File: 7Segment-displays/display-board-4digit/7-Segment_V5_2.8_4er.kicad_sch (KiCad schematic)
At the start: 3 parts, among them J1 Conn_02x08_Odd_Even, U1 HDSM-443B_CC_2Digit_7Segment_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, U2 HDSM-443B_CC_2Digit_7Segment_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

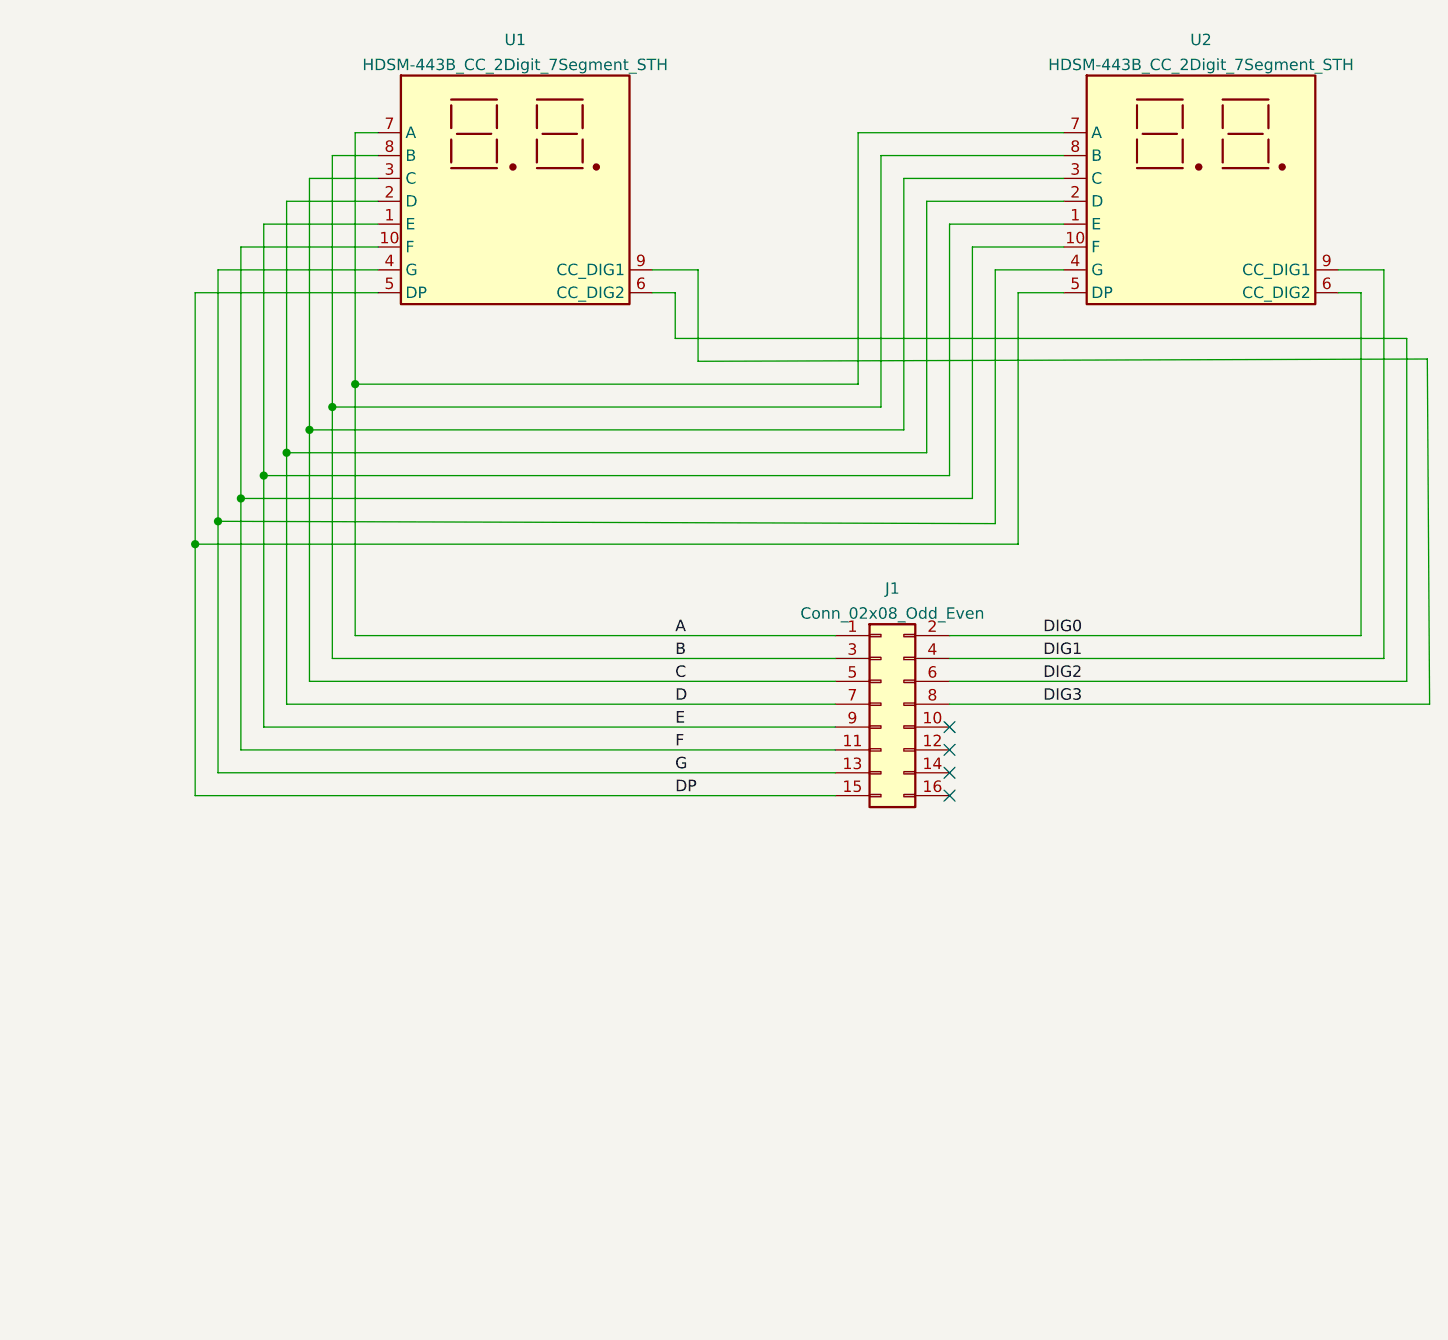
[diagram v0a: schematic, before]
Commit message: new symbol and footprint, connector rotated by 180 degree, new routing
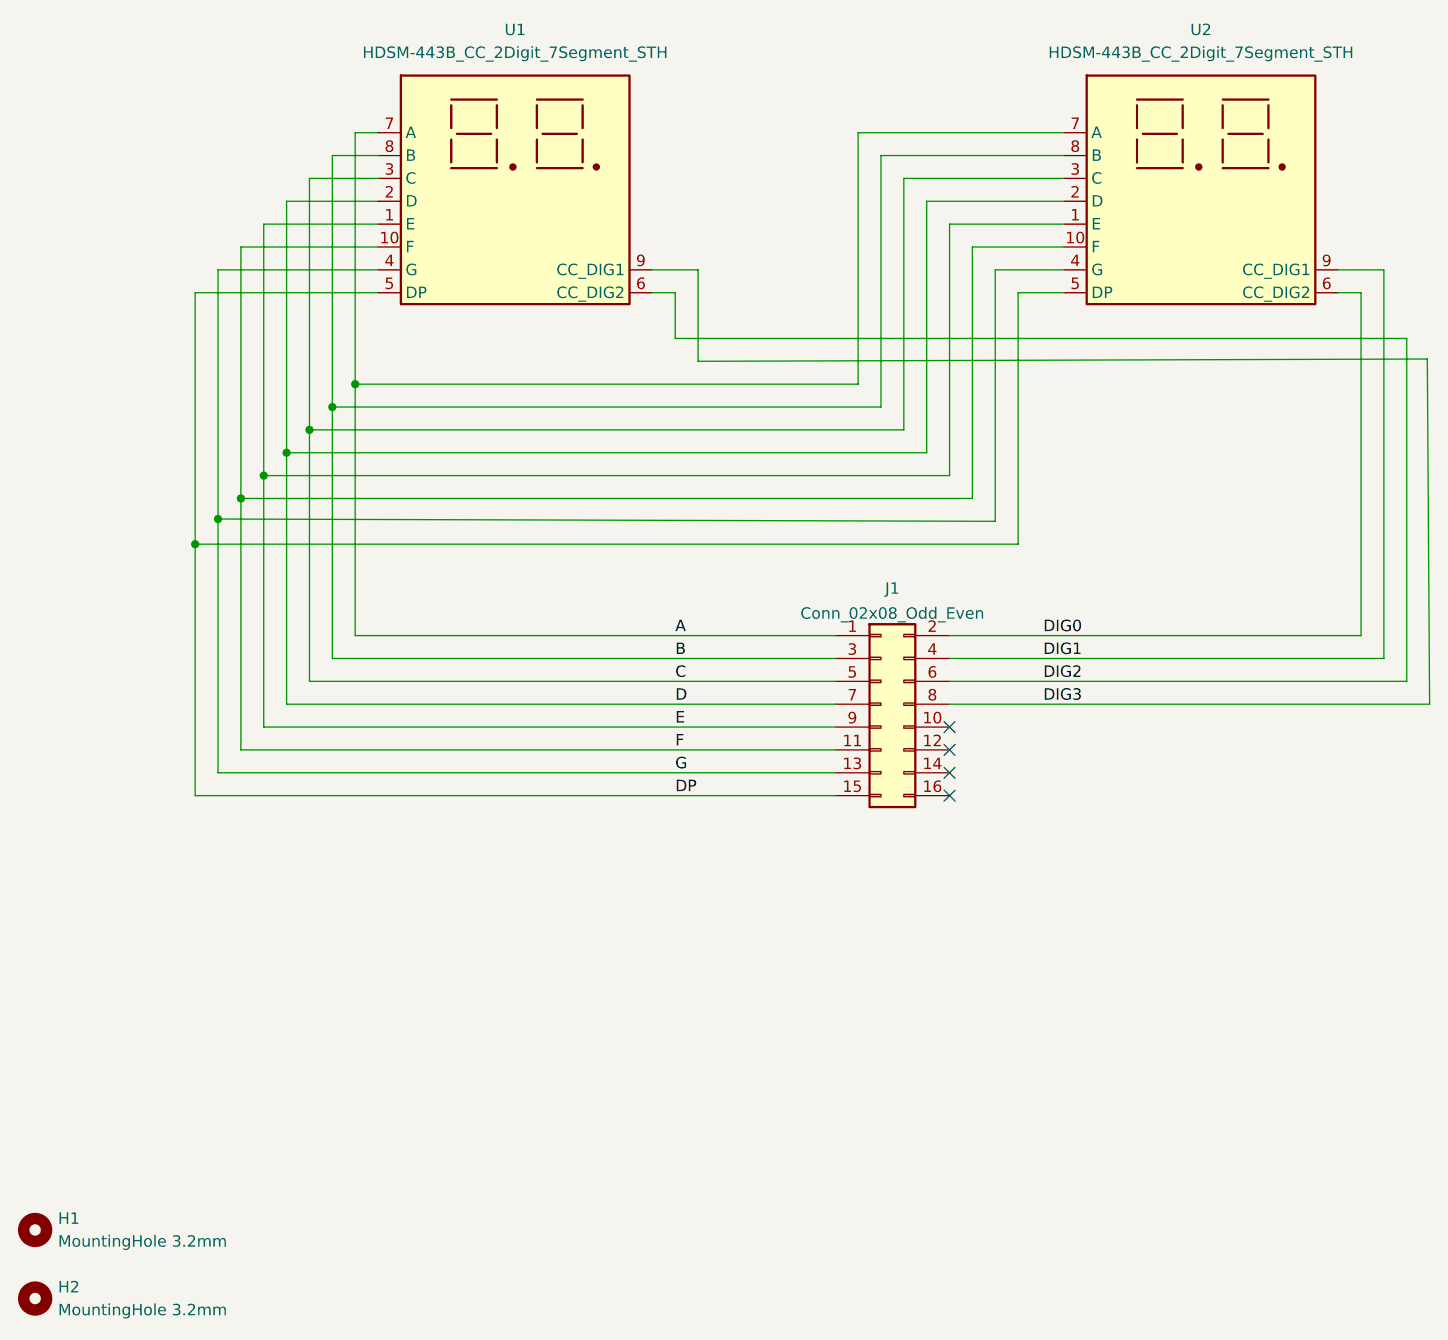
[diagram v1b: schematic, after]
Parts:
- added H1, H2: MountingHole 3.2mm, MountingHole:MountingHole_3.2mm_M3_Pad, symbol MobiFlight:MountingHole 3.2mm
- U1, U2: footprint Display_7Segment:STH_7_2 Digits_0.28_CC -> MobiFlight:STH_7_2 Digits_0.28_CC; symbol Display_Character:HDSM-443B_CC_2Digit_7Segment_STH -> MobiFlight:HDSM-443B_CC_2Digit_7Segment_STH
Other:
- company: (none) -> MobiFlight
- title: (none) -> 7 Segment Display Module, 4 digits
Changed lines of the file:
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@@
 	(generator_version "9.0")
 	(paper "A4")
+	(title_block
+		(title "7 Segment Display Module, 4 digits")
+		(date "2025-11-27")
+		(rev "V5.2")
+		(company "MobiFlight")
+	)
 	(junction
 		(at 73.66 73.66)
@@
 	)
 	(junction
-		(at 58.42 88.9)
+		(at 71.12 76.2)
 		(diameter 0)
 		(color 0 0 0 0)
 	)
 	(junction
-		(at 71.12 76.2)
+		(at 58.42 88.646)
 		(diameter 0)
 		(color 0 0 0 0)
@@
 	(wire
 		(pts
-			(xy 58.42 60.96) (xy 58.42 88.9)
+			(xy 58.42 60.96) (xy 58.42 88.646)
 		)
 		(stroke
@@
 	(wire
 		(pts
-			(xy 144.78 60.96) (xy 144.78 89.154)
+			(xy 144.78 60.96) (xy 144.78 88.9)
 		)
 		(stroke
@@
 	(wire
 		(pts
-			(xy 58.42 88.9) (xy 144.78 89.154)
+			(xy 58.42 88.646) (xy 144.78 88.9)
 		)
 		(stroke
@@
 	(wire
 		(pts
+			(xy 58.42 88.646) (xy 58.42 116.84)
+		)
+		(stroke
+			(width 0)
+			(type default)
+		)
+	)
+	(wire
+		(pts
 			(xy 182.88 63.5) (xy 185.42 63.5)
 		)
@@
 		(pts
 			(xy 132.08 76.2) (xy 71.12 76.2)
-		)
-		(stroke
-			(width 0)
-			(type default)
-		)
-	)
-	(wire
-		(pts
-			(xy 58.42 88.9) (xy 58.42 116.84)
 		)
 		(stroke
@@
 	)
 	(symbol
-		(lib_id "Display_Character:HDSM-443B_CC_2Digit_7Segment_STH")
+		(lib_id "MobiFlight:HDSM-443B_CC_2Digit_7Segment_STH")
 		(at 167.64 53.34 0)
 		(unit 1)
@@
 		(fields_autoplaced yes)
 		(property "Reference" "U2"
-			(at 167.64 35.4035 0)
+			(at 167.64 34.29 0)
 			(effects
 				(font
@@
 		)
 		(property "Value" "HDSM-443B_CC_2Digit_7Segment_STH"
-			(at 167.64 38.1786 0)
-			(effects
-				(font
-					(size 1.27 1.27)
-				)
-			)
-		)
-		(property "Footprint" "Display_7Segment:STH_7_2 Digits_0.28_CC"
+			(at 167.64 36.83 0)
+			(effects
+				(font
+					(size 1.27 1.27)
+				)
+			)
+		)
+		(property "Footprint" "MobiFlight:STH_7_2 Digits_0.28_CC"
 			(at 167.64 68.58 0)
 			(effects
@@
 				(path "/36760d4a-f556-46ce-84f1-a1c51caf80df"
 					(reference "U2")
+					(unit 1)
+				)
+			)
+		)
+	)
+	(symbol
+		(lib_id "MobiFlight:MountingHole 3.2mm")
+		(at 38.1 167.64 0)
+		(unit 1)
+		(exclude_from_sim yes)
+		(in_bom no)
+		(on_board yes)
+		(dnp no)
+		(fields_autoplaced yes)
+		(property "Reference" "H1"
+			(at 40.64 166.3699 0)
+			(effects
+				(font
+					(size 1.27 1.27)
+				)
+				(justify left)
+			)
+		)
+		(property "Value" "MountingHole 3.2mm"
+			(at 40.64 168.9099 0)
+			(effects
+				(font
+					(size 1.27 1.27)
+				)
+				(justify left)
+			)
+		)
+		(property "Footprint" "MountingHole:MountingHole_3.2mm_M3_Pad"
+			(at 38.1 167.64 0)
+			(effects
+				(font
+					(size 1.27 1.27)
+				)
+				(hide yes)
+			)
+		)
+		(property "Datasheet" "~"
+			(at 38.1 167.64 0)
+			(effects
+				(font
+					(size 1.27 1.27)
+				)
+				(hide yes)
+			)
+		)
+		(property "Description" "Mounting Hole without connection"
+			(at 38.1 167.64 0)
+			(effects
+				(font
+					(size 1.27 1.27)
+				)
+				(hide yes)
+			)
+		)
+		(instances
+			(project ""
+				(path "/36760d4a-f556-46ce-84f1-a1c51caf80df"
+					(reference "H1")
 					(unit 1)
 				)
@@
 	)
 	(symbol
-		(lib_id "Display_Character:HDSM-443B_CC_2Digit_7Segment_STH")
+		(lib_id "MobiFlight:HDSM-443B_CC_2Digit_7Segment_STH")
 		(at 91.44 53.34 0)
 		(unit 1)
@@
 		(fields_autoplaced yes)
 		(property "Reference" "U1"
-			(at 91.44 35.4035 0)
+			(at 91.44 34.29 0)
 			(effects
 				(font
@@
 		)
 		(property "Value" "HDSM-443B_CC_2Digit_7Segment_STH"
-			(at 91.44 38.1786 0)
-			(effects
-				(font
-					(size 1.27 1.27)
-				)
-			)
-		)
-		(property "Footprint" "Display_7Segment:STH_7_2 Digits_0.28_CC"
+			(at 91.44 36.83 0)
+			(effects
+				(font
+					(size 1.27 1.27)
+				)
+			)
+		)
+		(property "Footprint" "MobiFlight:STH_7_2 Digits_0.28_CC"
 			(at 91.44 68.58 0)
 			(effects
@@
 					(unit 1)
 				)
+			)
+		)
+	)
+	(symbol
+		(lib_id "MobiFlight:MountingHole 3.2mm")
+		(at 38.1 175.26 0)
+		(unit 1)
+		(exclude_from_sim yes)
+		(in_bom no)
+		(on_board yes)
+		(dnp no)
+		(fields_autoplaced yes)
+		(property "Reference" "H2"
+			(at 40.64 173.9899 0)
+			(effects
+				(font
+					(size 1.27 1.27)
+				)
+				(justify left)
+			)
+		)
+		(property "Value" "MountingHole 3.2mm"
+			(at 40.64 176.5299 0)
+			(effects
+				(font
+					(size 1.27 1.27)
+				)
+				(justify left)
+			)
+		)
+		(property "Footprint" "MountingHole:MountingHole_3.2mm_M3_Pad"
+			(at 38.1 175.26 0)
+			(effects
+				(font
+					(size 1.27 1.27)
+				)
+				(hide yes)
+			)
+		)
+		(property "Datasheet" "~"
+			(at 38.1 175.26 0)
+			(effects
+				(font
+					(size 1.27 1.27)
+				)
+				(hide yes)
+			)
+		)
+		(property "Description" "Mounting Hole without connection"
+			(at 38.1 175.26 0)
+			(effects
+				(font
+					(size 1.27 1.27)
+				)
+				(hide yes)
+			)
+		)
+		(instances
+			(project "7-Segment_V5_2.8_4er"
+				(path "/36760d4a-f556-46ce-84f1-a1c51caf80df"
+					(reference "H2")
+					(unit 1)
+				)

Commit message: update 4/5/6 digit schematic and pcb to MF lib, add 3 digit to lib
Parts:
- U1, U2: symbol MobiFlight:HDSM-443B_CC_2Digit_7Segment_STH -> MobiFlight:7Segment 2 digit common cathode STH
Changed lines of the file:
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@@
 	)
 	(symbol
-		(lib_id "MobiFlight:HDSM-443B_CC_2Digit_7Segment_STH")
+		(lib_id "MobiFlight:7Segment 2 digit common cathode STH")
 		(at 167.64 53.34 0)
 		(unit 1)
@@
 	)
 	(symbol
-		(lib_id "MobiFlight:HDSM-443B_CC_2Digit_7Segment_STH")
+		(lib_id "MobiFlight:7Segment 2 digit common cathode STH")
 		(at 91.44 53.34 0)
 		(unit 1)
